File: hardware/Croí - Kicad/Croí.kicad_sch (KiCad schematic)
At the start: 5 parts, among them J1 2060-1452/998-404, J2 ESQ-110-X-X-D, U1 NUP2105LT1G, U2 STM32F411CEUx

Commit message: minor junctions
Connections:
- net at U2.10 (PA0): now also CR1.1
- net at U2.11 (PA1): now also CR1.3, CR1.4
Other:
- moved on the sheet: CR1, J1, J2, U1, U2
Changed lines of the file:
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@@
 	(generator_version "9.0")
 	(paper "A4")
+	(junction
+		(at 93.98 64.77)
+		(diameter 0)
+		(color 0 0 0 0)
+	)
+	(wire
+		(pts
+			(xy 151.13 64.77) (xy 93.98 64.77)
+		)
+		(stroke
+			(width 0)
+			(type default)
+		)
+	)
+	(wire
+		(pts
+			(xy 118.11 25.4) (xy 111.76 25.4)
+		)
+		(stroke
+			(width 0)
+			(type default)
+		)
+	)
+	(wire
+		(pts
+			(xy 93.98 64.77) (xy 68.58 64.77)
+		)
+		(stroke
+			(width 0)
+			(type default)
+		)
+	)
+	(wire
+		(pts
+			(xy 111.76 25.4) (xy 111.76 62.23)
+		)
+		(stroke
+			(width 0)
+			(type default)
+		)
+	)
+	(wire
+		(pts
+			(xy 93.98 35.56) (xy 93.98 64.77)
+		)
+		(stroke
+			(width 0)
+			(type default)
+		)
+	)
+	(wire
+		(pts
+			(xy 111.76 62.23) (xy 68.58 62.23)
+		)
+		(stroke
+			(width 0)
+			(type default)
+		)
+	)
+	(wire
+		(pts
+			(xy 151.13 35.56) (xy 151.13 64.77)
+		)
+		(stroke
+			(width 0)
+			(type default)
+		)
+	)
+	(wire
+		(pts
+			(xy 118.11 35.56) (xy 93.98 35.56)
+		)
+		(stroke
+			(width 0)
+			(type default)
+		)
+	)
 	(symbol
 		(lib_id "ESQ:ESQ-110-X-X-D")
-		(at 212.09 60.96 0)
+		(at 184.15 46.99 0)
 		(unit 1)
 		(exclude_from_sim no)
@@
 		(fields_autoplaced yes)
 		(property "Reference" "J2"
-			(at 212.09 43.18 0)
+			(at 184.15 29.21 0)
 			(effects
 				(font
@@
 		)
 		(property "Value" "ESQ-110-X-X-D"
-			(at 212.09 45.72 0)
+			(at 184.15 31.75 0)
 			(effects
 				(font
@@
 		)
 		(property "Footprint" "SAMTEC_ESQ-110-14-G-D"
-			(at 212.09 60.96 0)
+			(at 184.15 46.99 0)
 			(effects
 				(font
@@
 		)
 		(property "Datasheet" ""
-			(at 212.09 60.96 0)
+			(at 184.15 46.99 0)
 			(effects
 				(font
@@
 		)
 		(property "Description" ""
-			(at 212.09 60.96 0)
+			(at 184.15 46.99 0)
 			(effects
 				(font
@@
 		)
 		(property "MF" "Samtec"
-			(at 212.09 60.96 0)
+			(at 184.15 46.99 0)
 			(effects
 				(font
@@
 		)
 		(property "Description_1" "20 Position Elevated Socket Connector 0.100 (2.54mm) Through Hole Gold"
-			(at 212.09 60.96 0)
+			(at 184.15 46.99 0)
 			(effects
 				(font
@@
 		)
 		(property "Package" "None"
-			(at 212.09 60.96 0)
+			(at 184.15 46.99 0)
 			(effects
 				(font
@@
 		)
 		(property "Price" "None"
-			(at 212.09 60.96 0)
+			(at 184.15 46.99 0)
 			(effects
 				(font
@@
 		)
 		(property "Check_prices" "https://www.snapeda.com/parts/ESQ-110-14-G-D-LL/Samtec/view-part/?ref=eda"
-			(at 212.09 60.96 0)
+			(at 184.15 46.99 0)
 			(effects
 				(font
@@
 		)
 		(property "STANDARD" "Manufacturer Recommendations"
-			(at 212.09 60.96 0)
+			(at 184.15 46.99 0)
 			(effects
 				(font
@@
 		)
 		(property "PARTREV" "NA"
-			(at 212.09 60.96 0)
+			(at 184.15 46.99 0)
 			(effects
 				(font
@@
 		)
 		(property "SnapEDA_Link" "https://www.snapeda.com/parts/ESQ-110-14-G-D-LL/Samtec/view-part/?ref=snap"
-			(at 212.09 60.96 0)
+			(at 184.15 46.99 0)
 			(effects
 				(font
@@
 		)
 		(property "MP" "ESQ-110-14-G-D-LL"
-			(at 212.09 60.96 0)
+			(at 184.15 46.99 0)
 			(effects
 				(font
@@
 		)
 		(property "Purchase-URL" "https://www.snapeda.com/api/url_track_click_mouser/?unipart_id=3563488&manufacturer=Samtec&part_name=ESQ-110-14-G-D-LL&search_term=esq-110-14-g-d-ll"
-			(at 212.09 60.96 0)
+			(at 184.15 46.99 0)
 			(effects
 				(font
@@
 		)
 		(property "Availability" "In Stock"
-			(at 212.09 60.96 0)
+			(at 184.15 46.99 0)
 			(effects
 				(font
@@
 		)
 		(property "MANUFACTURER" "Samtec"
-			(at 212.09 60.96 0)
+			(at 184.15 46.99 0)
 			(effects
 				(font
@@
 	(symbol
 		(lib_id "1:NUP2105LT1G")
-		(at 66.04 109.22 0)
+		(at 101.6 135.89 0)
 		(unit 1)
 		(exclude_from_sim no)
@@
 		(fields_autoplaced yes)
 		(property "Reference" "U1"
-			(at 86.36 99.06 0)
+			(at 121.92 125.73 0)
 			(effects
 				(font
@@
 		)
 		(property "Value" "NUP2105LT1G"
-			(at 86.36 101.6 0)
+			(at 121.92 128.27 0)
 			(effects
 				(font
@@
 		)
 		(property "Footprint" "SOT-23_3L_ONS"
-			(at 66.04 109.22 0)
+			(at 101.6 135.89 0)
 			(effects
 				(font
@@
 		)
 		(property "Datasheet" "NUP2105LT1G"
-			(at 66.04 109.22 0)
+			(at 101.6 135.89 0)
 			(effects
 				(font
@@
 		)
 		(property "Description" ""
-			(at 66.04 109.22 0)
+			(at 101.6 135.89 0)
 			(effects
 				(font
@@
 	(symbol
 		(lib_id "MCU_ST_STM32F4:STM32F411CEUx")
-		(at 55.88 57.15 0)
+		(at 50.8 97.79 0)
 		(unit 1)
 		(exclude_from_sim no)
@@
 		(fields_autoplaced yes)
 		(property "Reference" "U2"
-			(at 60.5633 97.79 0)
+			(at 55.4833 138.43 0)
 			(effects
 				(font
@@
 		)
 		(property "Value" "STM32F411CEUx"
-			(at 60.5633 100.33 0)
+			(at 55.4833 140.97 0)
 			(effects
 				(font
@@
 		)
 		(property "Footprint" "Package_DFN_QFN:QFN-48-1EP_7x7mm_P0.5mm_EP5.6x5.6mm"
-			(at 40.64 95.25 0)
+			(at 35.56 135.89 0)
 			(effects
 				(font
@@
 		)
 		(property "Datasheet" "https://www.st.com/resource/en/datasheet/stm32f411ce.pdf"
-			(at 55.88 57.15 0)
+			(at 50.8 97.79 0)
 			(effects
 				(font
@@
 		)
 		(property "Description" "STMicroelectronics Arm Cortex-M4 MCU, 512KB flash, 128KB RAM, 100 MHz, 1.7-3.6V, 36 GPIO, UFQFPN48"
-			(at 55.88 57.15 0)
+			(at 50.8 97.79 0)
 			(effects
 				(font
@@
 	(symbol
 		(lib_id "usb:USBLC6-2SC6")
-		(at 111.76 48.26 0)
+		(at 118.11 25.4 0)
 		(unit 1)
 		(exclude_from_sim no)
@@
 		(fields_autoplaced yes)
 		(property "Reference" "CR1"
-			(at 128.27 40.64 0)
+			(at 134.62 17.78 0)
 			(effects
 				(font
@@
 		)
 		(property "Value" "USBLC6-2SC6"
-			(at 128.27 43.18 0)
+			(at 134.62 20.32 0)
 			(effects
 				(font
@@
 		)
 		(property "Footprint" "SOT23-6L_STM"
-			(at 111.76 48.26 0)
+			(at 118.11 25.4 0)
 			(effects
 				(font
@@
 		)
 		(property "Datasheet" "https://www.st.com/resource/en/datasheet/usblc6-2.pdf"
-			(at 111.76 48.26 0)
+			(at 118.11 25.4 0)
 			(effects
 				(font
@@
 		)
 		(property "Description" ""
-			(at 111.76 48.26 0)
+			(at 118.11 25.4 0)
 			(effects
 				(font
@@
 	(symbol
 		(lib_id "wago:2060-1452_998-404")
-		(at 146.05 86.36 0)
+		(at 64.77 30.48 0)
 		(unit 1)
 		(exclude_from_sim no)
@@
 		(fields_autoplaced yes)
 		(property "Reference" "J1"
-			(at 160.02 88.8999 0)
+			(at 78.74 33.0199 0)
 			(effects
 				(font
@@
 		)
 		(property "Value" "2060-1452/998-404"
-			(at 160.02 91.4399 0)
+			(at 78.74 35.5599 0)
 			(effects
 				(font
@@
 		)
 		(property "Footprint" "WAG"
-			(at 146.05 86.36 0)
+			(at 64.77 30.48 0)
 			(effects
 				(font
@@
 		)
 		(property "Datasheet" "2060-1452/998-404"
-			(at 146.05 86.36 0)
+			(at 64.77 30.48 0)
 			(effects
 				(font
@@
 		)
 		(property "Description" ""
-			(at 146.05 86.36 0)
-			(effects
-				(font
+			(at 64.77 30.48 0)
+			(effects
+				(font

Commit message: did basically all of it
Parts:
- removed CR1: USBLC6-2SC6, SOT23-6L_STM, symbol usb:USBLC6-2SC6
- removed J2: ESQ-110-X-X-D, SAMTEC_ESQ-110-14-G-D, symbol ESQ:ESQ-110-X-X-D
- removed U1: NUP2105LT1G, SOT-23_3L_ONS, symbol 1:NUP2105LT1G
- removed U2: STM32F411CEUx, Package_DFN_QFN:QFN-48-1EP_7x7mm_P0.5mm_EP5.6x5.6mm, symbol MCU_ST_STM32F4:STM32F411CEUx
- added C10: 1uF, Capacitor_SMD:C_0402_1005Metric, symbol Device:C
- added C12: 10nF, Capacitor_SMD:C_0402_1005Metric, symbol Device:C
- added C15, C2: 4.7 uF, Capacitor_SMD:C_0402_1005Metric, symbol Device:C
- added C17, C4, C6, C7, C8: 100 nF, Capacitor_SMD:C_0402_1005Metric, symbol Device:C
- added C18, C19, C20, C21, C22, C25, C5: 100nF, Capacitor_SMD:C_0402_1005Metric, symbol Device:C
- added C23: 1 uF, Capacitor_SMD:C_0402_1005Metric, symbol Device:C
- added C24, C26: 47 uF, Capacitor_SMD:C_0402_1005Metric, symbol Device:C
- added D1: BAT54C, Package_TO_SOT_SMD:SOT-23, symbol Diode:BAT54C
- added D2: NUP2105L, Package_TO_SOT_SMD:SOT-23, symbol Power_Protection:NUP2105L
- added J1: Conn_ARM_JTAG_SWD_10, symbol Connector:Conn_ARM_JTAG_SWD_10
- added J3: ESQ-110-14-G-D, Connector_PinHeader_2.54mm:PinHeader_2x10_P2.54mm_Vertical, symbol ESQ-110-X-X-D:ESQ-110-X-X-D
- added J4: Conn_02x03_Odd_Even, Connector_PinHeader_1.00mm:PinHeader_2x03_P1.00mm_Vertical, symbol Connector_Generic:Conn_02x03_Odd_Even
- added J5: USB_C_Receptacle_USB2.0_16P, Connector_USB:USB_C_Receptacle_G-Switch_GT-USB-7010ASV, symbol Connector:USB_C_Receptacle_USB2.0_16P
- added R2, R5: 10K, Resistor_SMD:R_0402_1005Metric, symbol Device:R
- added R3, R4: 5.1K, Resistor_SMD:R_0402_1005Metric, symbol Device:R
- added R6, R7: 60 Ω, Resistor_SMD:R_0402_1005Metric, symbol Device:R
- added U1: W25Q128JVS, Package_SO:SOIC-8_5.3x5.3mm_P1.27mm, symbol Memory_Flash:W25Q128JVS
- added U3: STM32F072C8Tx, Package_QFP:LQFP-48_7x7mm_P0.5mm, symbol MCU_ST_STM32F0:STM32F072C8Tx
- added U4: BME680, footprints:LGA8_BME680_BOS, symbol BME680:BME680
- added U5: BMP390, footprints:10LGA_2X2X0p75_BOS, symbol BMP390:BMP390
- added U6: USBLC6-2SC6, Package_TO_SOT_SMD:SOT-23-6, symbol Power_Protection:USBLC6-2SC6
- added U7: TLV70433DBVT, TLV70433DBVT:DBV0005A_N, symbol TLV70433DBVT:TLV70433DBVT
- added U8: TJA1051T-3, Package_SO:SOIC-8_3.9x4.9mm_P1.27mm, symbol Interface_CAN_LIN:TJA1051T-3
- J2: renamed from J1; footprint WAG -> footprints:WAG
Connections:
- net VBAT: now reaches J2.1 (1_1)
- net VBAT: now also J2.2 (1_2), D1.2
- net GND: now reaches J2.3 (2_1)
- net GND: now also J2.4 (2_2), C10.2, C12.2, C15.2, C17.2, C18.2, C19.2, C2.2, C20.2, C21.2, C23.1, C24.2, C25.2, C26.2, C4.2, C5.2, C6.2, C7.2, C8.2, D2.3 (A), J1.3 (GND), J1.5 (GND), J1.9 (GNDDetect), J3.01, J3.02, J3.07, J3.08, J3.13, J3.14, J3.17, J3.18, J3.19, J3.20, J5.A1 (GND), J5.A12 (GND), J5.B1 (GND), J5.B12 (GND), J5.S1 (SHIELD), R3.1, R4.2, R5.1, U1.4 (GND), U3.23 (VSS), U3.35 (VSS), U3.47 (VSS), U3.8 (VSSA), U4.1, U4.7, U5.3 (VSS), U5.8 (VSS), U5.9 (VSS), U6.2 (GND), U7.1 (GND), U7.4 (NC), U7.5 (NC), U8.2 (GND), U8.8 (S)
- new net: C21.1, D1.3, U7.2 (IN)
- new net: J5.A7 (D-), J5.B7 (D-), U6.4 (I/O2)
- new net: J5.A6 (D+), J5.B6 (D+), U6.6 (I/O1)
- new net: J5.B5 (CC2), R3.2
- new net: C26.1, R6.2, R7.1
- new net: J5.A5 (CC1), R4.1
- new net 3.3V: C10.1, C12.1, C15.1, C17.1, C18.1, C19.1, C2.1, C20.1, C22.1, C23.2, C4.1, C5.1, C6.1, C7.1, C8.1, J1.1 (VTref), U1.3 (~{WP}/IO_{2}), U1.7 (~{HOLD}/~{RESET}/IO_{3}), U1.8 (VCC), U3.1 (VBAT), U3.24 (VDD), U3.36 (VDDIO2), U3.48 (VDD), U3.9 (VDDA), U4.6, U4.8, U5.1 (VDDIO), U5.10 (VDD), U7.3 (OUT), U8.5 (VIO)
- new net 5VLOGIC: C22.2, C24.1, C25.1, J3.03, J3.04, J3.05, J3.06, U8.3 (VCC)
- new net 5VSERVO: J3.09, J3.10, J3.11, J3.12
- new net BME680_CS: U3.27 (PB14), U4.2
- new net BMP390_CS: U3.40 (PB4), U5.6 (CSB)
- new net CAN+: J4.2 (Pin_2), U8.1 (TXD)
- new net CAN-: J4.1 (Pin_1), U8.4 (RXD)
- new net CAN_out+: D2.1 (K), J3.16, R6.1, U8.7 (CANH)
- new net CAN_out-: D2.2 (K), J3.15, R7.2, U8.6 (CANL)
- new net Flash_CS: U1.1 (~{CS}), U3.25 (PB12)
- new net Mode_sel: R2.1, R5.2, U3.26 (PB13)
- new net NRST: J1.10 (~{RESET}), U3.7 (NRST)
- new net PA+: J4.4 (Pin_4), U3.33 (PA12)
- new net PA-: J4.3 (Pin_3), U3.32 (PA11)
- new net SPI_MISO: U1.5 (DI/IO_{0}), U3.16 (PA6), U4.5, U5.5 (SDO)
- new net SPI_MOSI: U1.2 (DO/IO_{1}), U3.17 (PA7), U4.3, U5.4 (SDI)
- new net SWCLK: J1.4 (SWCLK/TCK), U1.6 (CLK), U3.37 (PA14), U4.4, U5.2 (SCK)
- new net SWDIO: J1.2 (SWDIO/TMS), U3.34 (PA13)
- new net USB_D+: J4.6 (Pin_6), U6.1 (I/O1)
- new net USB_D-: J4.5 (Pin_5), U6.3 (I/O2)
- new net VBUS_RAW: D1.1, J5.A4 (VBUS), J5.A9 (VBUS), J5.B4 (VBUS), J5.B9 (VBUS), R2.2, U6.5 (VBUS)
- no-connect marks 0 -> 5
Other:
- note added: "Flash"
- note added: "USB-C & mode select"
- note added: "interboard connector"
- moved on the sheet: J2

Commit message: started pcb work
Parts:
- J1: footprint (none) -> Connector_PinHeader_1.27mm:PinHeader_2x05_P1.27mm_Vertical
- U7: footprint TLV70433DBVT:DBV0005A_N -> footprints:DBV0005A_M
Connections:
- net SWCLK: no longer U1.6 (CLK), U4.4, U5.2 (SCK)
- net SPICLK: now reaches U3.15 (PA5)
- net SPICLK: now also U1.6 (CLK), U4.4, U5.2 (SCK)
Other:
- moved on the sheet: C5, J2, U1

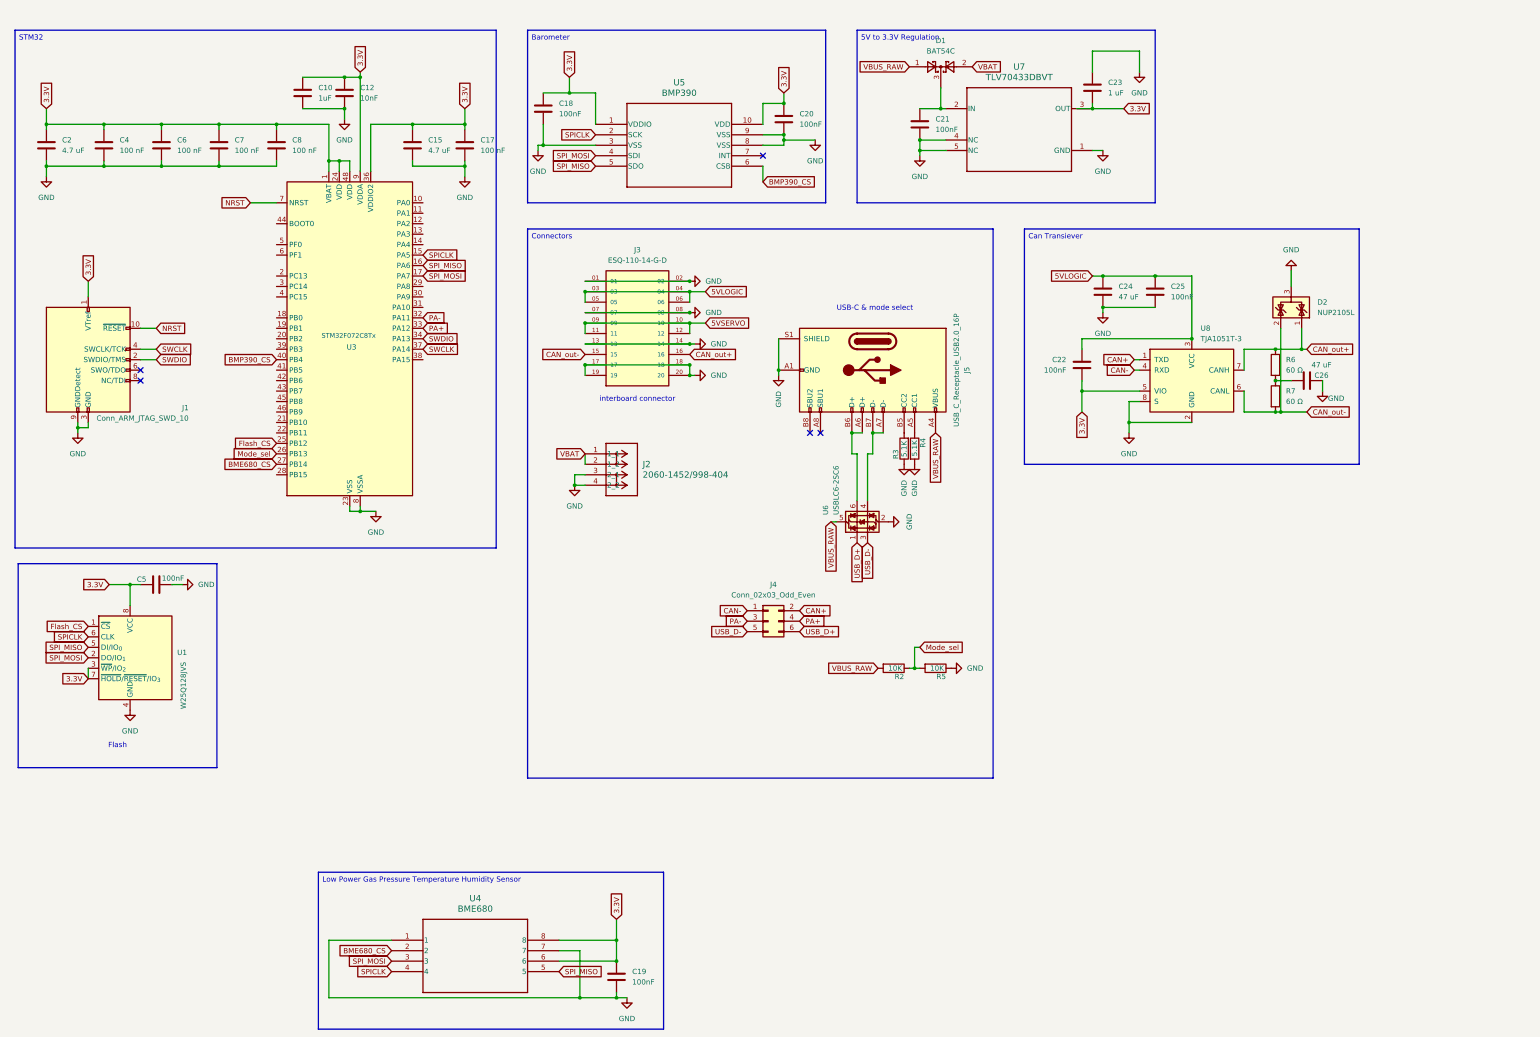
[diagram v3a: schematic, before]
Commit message: Finalised board with accelerometer and IMU
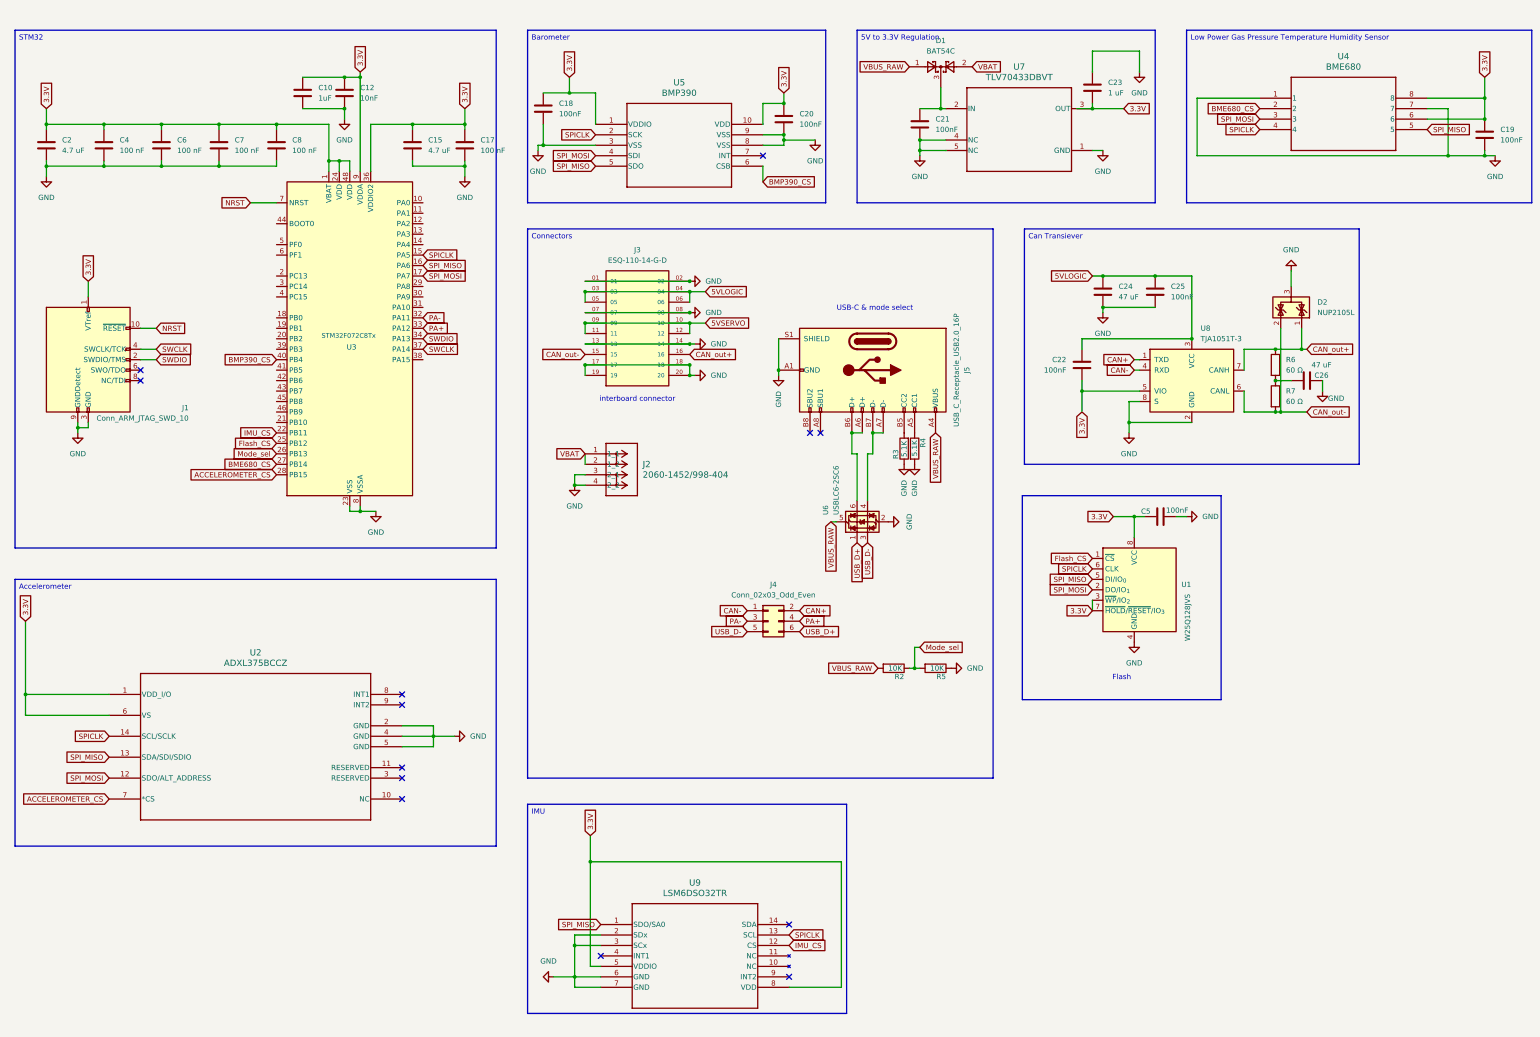
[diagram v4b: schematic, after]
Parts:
- added U2: ADXL375BCCZ, LGA_CC-14-1_ADI, symbol ADXL375BCCZ:ADXL375BCCZ
- added U9: LSM6DSO32TR, LGA-14L_2P5X3X0P83_STM, symbol LSM6DSO32TR:LSM6DSO32TR
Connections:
- net 3.3V: now also U2.1 (VDD_I/O), U2.6 (VS), U9.5 (VDDIO), U9.8 (VDD)
- net GND: now also U2.2 (GND), U2.4 (GND), U2.5 (GND), U9.2 (SDx), U9.3 (SCx), U9.6 (GND), U9.7 (GND)
- net SPICLK: now also U2.14 (SCL/SCLK), U9.13 (SCL)
- net SPI_MISO: now also U2.13 (SDA/SDI/SDIO), U9.1 (SDO/SA0)
- net SPI_MOSI: now also U2.12 (SDO/ALT_ADDRESS)
- net IMU_CS: now reaches U3.22 (PB11)
- net IMU_CS: now also U9.12 (CS)
- net ACCELEROMETER_CS: now reaches U3.28 (PB15)
- net ACCELEROMETER_CS: now also U2.7 (*CS)
- no-connect marks 5 -> 13
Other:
- moved on the sheet: C19, C5, U1, U4

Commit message: summaries are hard
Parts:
- removed J1: Conn_ARM_JTAG_SWD_10, Connector_PinHeader_1.27mm:PinHeader_2x05_P1.27mm_Vertical, symbol Connector:Conn_ARM_JTAG_SWD_10
- added C1, C9: 100nF, Capacitor_SMD:C_0402_1005Metric, symbol Device:C
- added C11, C3: 1uF, Capacitor_SMD:C_0402_1005Metric, symbol Device:C
- added J6: Conn_02x03_Odd_Even, Connector_PinHeader_1.00mm:PinHeader_2x03_P1.00mm_Vertical, symbol Connector_Generic:Conn_02x03_Odd_Even
- added Q1: IPP060N06N, Package_TO_SOT_THT:TO-220-3_Vertical, symbol Transistor_FET:IPP060N06N
- J3: footprint Connector_PinHeader_2.54mm:PinHeader_2x10_P2.54mm_Vertical -> footprints:SAMTEC_ESQ-110-14-G-D
- U2: footprint LGA_CC-14-1_ADI -> footprints:LGA_CC-14-1_ADI
- U9: footprint LGA-14L_2P5X3X0P83_STM -> footprints:LGA-14L_2P5X3X0P83_STM
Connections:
- net 3.3V: now also C1.1, C11.2, C3.1, C9.2, J6.6 (Pin_6)
- net GND: now also C1.2, C11.1, C3.2, C9.1, J6.3 (Pin_3), J6.5 (Pin_5), Q1.1 (G)
- net NRST: now also J6.1 (Pin_1)
- net SWCLK: now also J6.4 (Pin_4)
- net SWDIO: now also J6.2 (Pin_2)
- net VBAT: now also Q1.3 (S); no longer J2.1 (1_1), J2.2 (1_2)
- removed net 5VSERVO: J3.09, J3.10, J3.11, J3.12
- new net: J2.1 (1_1), J2.2 (1_2), Q1.2 (D)
- no-connect marks 13 -> 40
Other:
- note removed: "Flash"
- moved on the sheet: C22, C24, C25, C26, C5, D2, J2, J3, J4, J5, R2, R3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

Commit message: changed some stuff
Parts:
- removed D1: BAT54C, Package_TO_SOT_SMD:SOT-23, symbol Diode:BAT54C
- removed J4, J6: Conn_02x03_Odd_Even, Connector_PinHeader_1.00mm:PinHeader_2x03_P1.00mm_Vertical, symbol Connector_Generic:Conn_02x03_Odd_Even
- removed J5: USB_C_Receptacle_USB2.0_16P, Connector_USB:USB_C_Receptacle_G-Switch_GT-USB-7010ASV, symbol Connector:USB_C_Receptacle_USB2.0_16P
- removed R2, R5: 10K, Resistor_SMD:R_0402_1005Metric, symbol Device:R
- removed R3, R4: 5.1K, Resistor_SMD:R_0402_1005Metric, symbol Device:R
- removed U6: USBLC6-2SC6, Package_TO_SOT_SMD:SOT-23-6, symbol Power_Protection:USBLC6-2SC6
- added J1: JTAG-10 PIN, Connector_IDC:IDC-Header_2x05_P2.54mm_Vertical, symbol Connector_Generic_MountingPin:Conn_01x10_MountingPin
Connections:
- net PA+ is gone; now on net CAN+: U3.33 (PA12)
- net PA- is gone; now on net CAN-: U3.32 (PA11)
- net 3.3V: now also J1.7 (Pin_7), J1.8 (Pin_8)
- net 5VLOGIC: no longer J3.03, J3.04
- net CAN_out-: now also J3.18; no longer J3.15
- net GND: now also J3.03, J3.04, J1.5 (Pin_5), J1.6 (Pin_6); no longer J3.01, J3.02, J3.13, J3.17, J3.18
- net NRST: now also J3.10, J1.1 (Pin_1)
- net SWCLK: now also J3.17, J1.2 (Pin_2)
- net SWDIO: now also J3.15, J1.4 (Pin_4)
- net VBAT: now also C21.1, U7.2 (IN)
- no-connect marks 40 -> 44
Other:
- note added: "Connector_IDC:IDC-Header_2x05_P2.54mm_Vertical"
- note removed: "USB-C & mode select"
